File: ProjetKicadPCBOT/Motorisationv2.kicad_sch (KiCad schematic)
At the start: 8 parts, among them J4 Screw_Terminal_01x02, J5 Screw_Terminal_01x02, U3 DRV8411APWPR

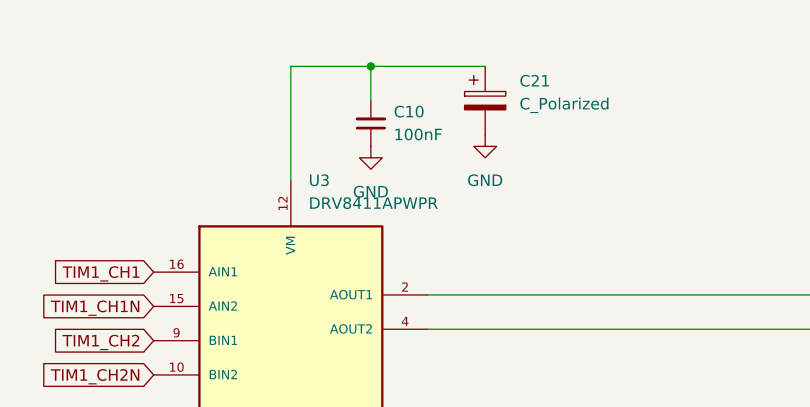
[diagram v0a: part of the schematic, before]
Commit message: Il reste 6 warning et il faut arranger les écritures
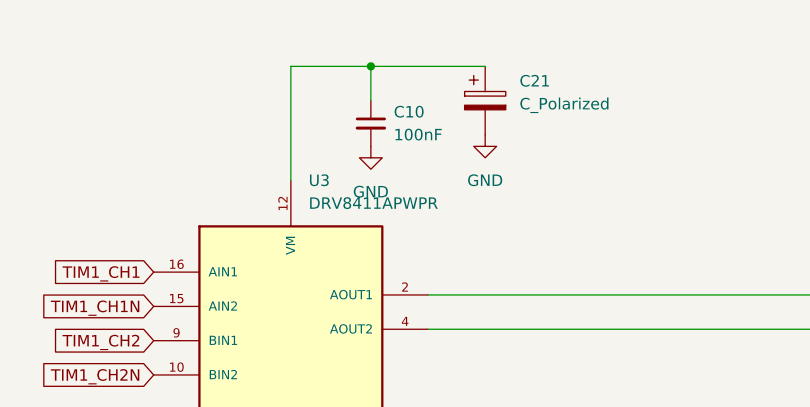
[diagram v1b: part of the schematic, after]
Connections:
- net GND: now also C10.2; no longer C10.1
- net at C21.1, U3.12 (VM): now also C10.1; no longer C10.2
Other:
- moved on the sheet: C10
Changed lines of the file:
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@@
 	(symbol
 		(lib_id "PCBot_Lib:C_Small")
-		(at 129.54 71.12 180)
+		(at 129.54 71.12 0)
 		(unit 1)
 		(exclude_from_sim no)
@@
 		(fields_autoplaced yes)
 		(property "Reference" "C10"
-			(at 132.08 69.8435 0)
+			(at 132.08 69.8562 0)
 			(effects
 				(font
 					(size 1.27 1.27)
 				)
-				(justify right)
+				(justify left)
 			)
 		)
 		(property "Value" "100nF"
-			(at 132.08 72.3835 0)
+			(at 132.08 72.3962 0)
 			(effects
 				(font
 					(size 1.27 1.27)
 				)
-				(justify right)
+				(justify left)
 			)
 		)

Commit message: .
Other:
- company: (none) -> ENSEA
- title: (none) -> PCB BOT rahim 974
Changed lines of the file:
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@@
 	(generator_version "9.0")
 	(paper "A4")
+	(title_block
+		(title "PCB BOT rahim 974")
+		(date "2026-02-07")
+		(rev "1.0")
+		(company "ENSEA")
+	)
 	(text "MOTEUR 1\n"
 		(exclude_from_sim no)
